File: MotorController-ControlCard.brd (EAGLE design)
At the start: 71.9 x 61 mm, 46 parts, among them J1 SL07-HORIZ, J2 SL03THROUGH_HOLE, Q7 MOSFET-PCHANNEL, Q8 MOSFET-PCHANNEL, U2 MAX3232D, U4 TMS320F28069MPZT

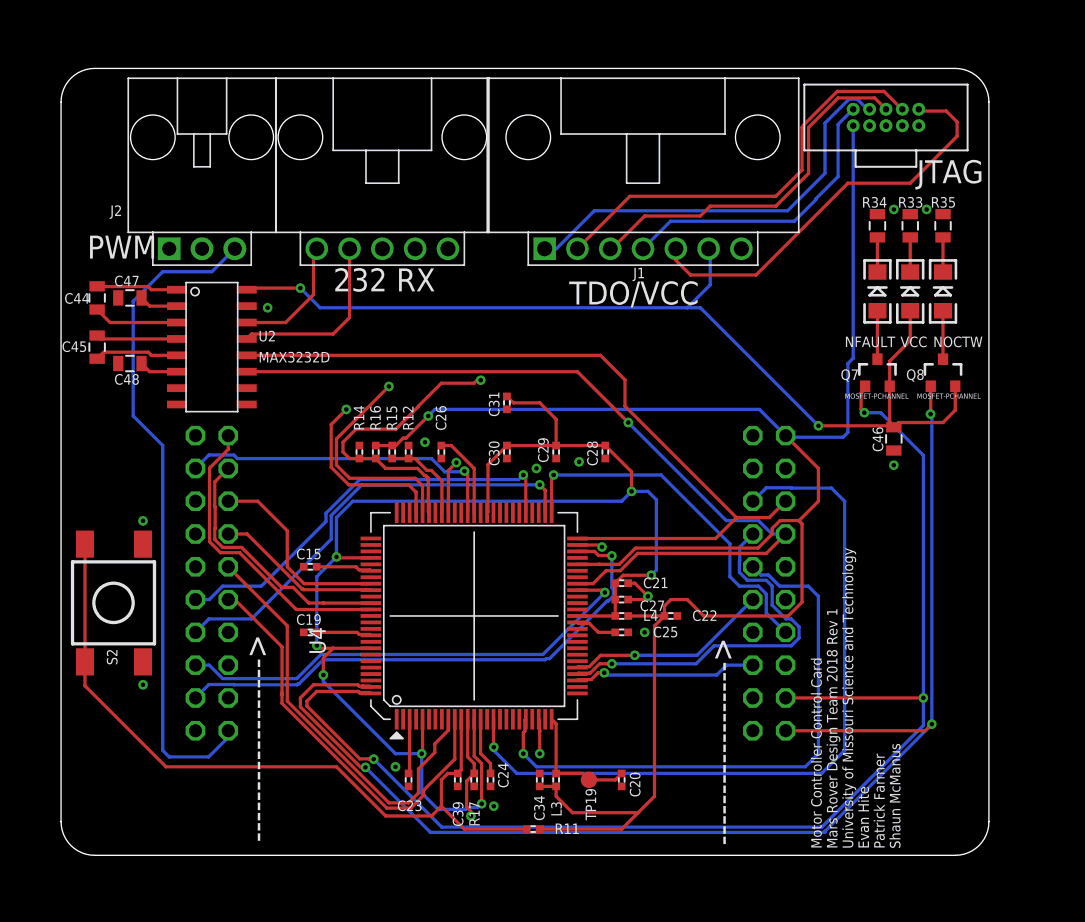
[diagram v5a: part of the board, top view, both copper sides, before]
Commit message: Routing and Silkscreen update
SL connectors were shifted apart to better mount them. Silkcreen was added around LED's for better visibility. Board was rerouted to get the board down to two layers.
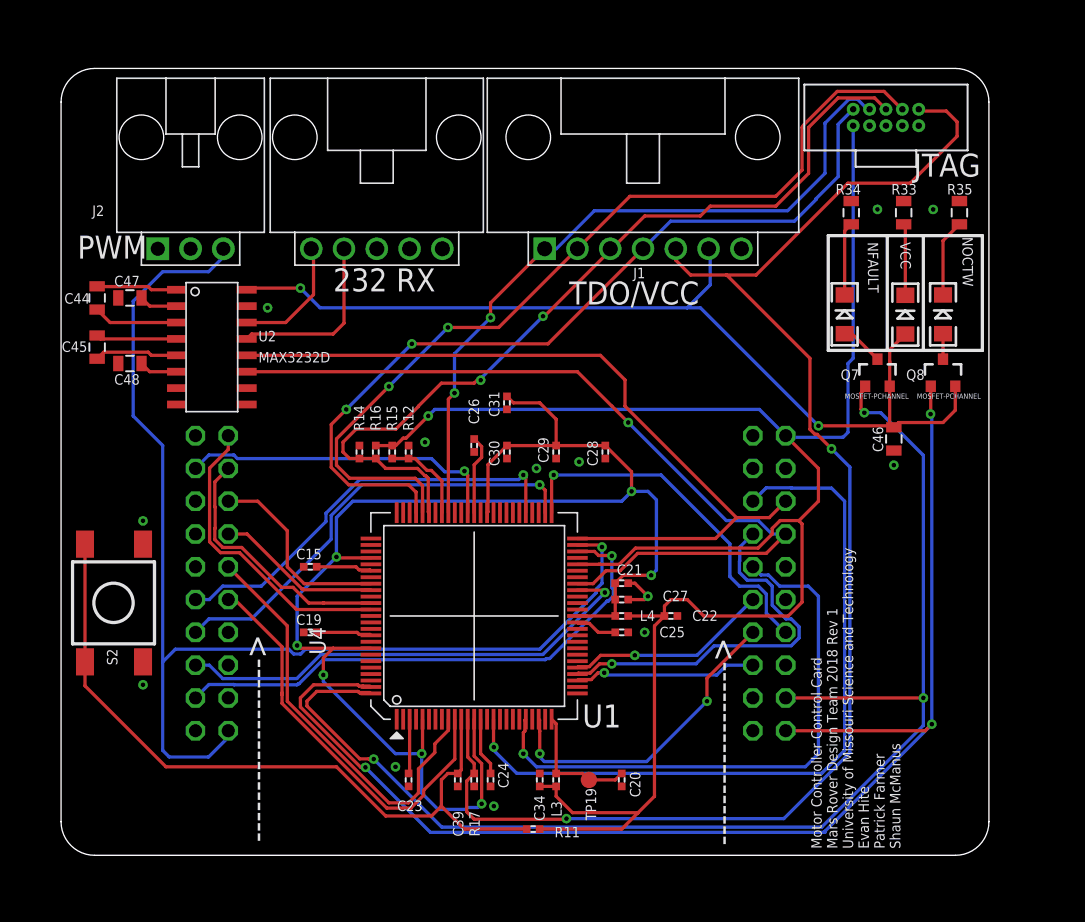
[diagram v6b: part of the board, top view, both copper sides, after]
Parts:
- moved D8 3.10 mm to (123.4, 81.3)
- moved C26 2.59 mm to (94.7, 71.1)
- moved R34 2.27 mm to (124.0, 89.2)
- moved D7 1.84 mm to (128.1, 81.3)
- moved D9 1.78 mm to (131.1, 81.3)
- moved R35 1.63 mm to (132.3, 89.2)
- moved R33 1.14 mm to (128.0, 89.2)
- moved J2 0.89 mm to (72.8, 86.4)
- moved U$4 0.43 mm to (87.2, 86.4)
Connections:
- net GND: now also U$2.7
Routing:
- net TRST: track 99.9 -> 112.8 mm, vias 1 -> 2
- net PWM_IN: track 88.6 -> 93.0 mm
- net TMS: track 69.3 -> 65.2 mm, vias 1 -> 2
- net TDI: track 72.4 -> 69.0 mm, vias 1 -> 2
- net N$27: track 2.68 -> 6.00 mm
- net N$26: track 2.68 -> 5.68 mm
- net N$24: track 2.68 -> 5.55 mm
- net VDDIO: track 113.1 -> 115.2 mm
- net SO1: track 26.7 -> 24.8 mm, vias 1 -> 2
- net N$28: track 3.75 -> 1.97 mm
- net VCC: track 77.0 -> 75.2 mm
- net N$16: track 6.70 -> 6.19 mm
- net TDO: track 66.6 -> 66.7 mm, vias 1 -> 2
- net TCK: track 56.2 -> 56.1 mm, vias 1 -> 2
- removed copper zone on layer 15, net GND
- removed copper zone on layer 2, net GND
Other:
- board text added: "U1"

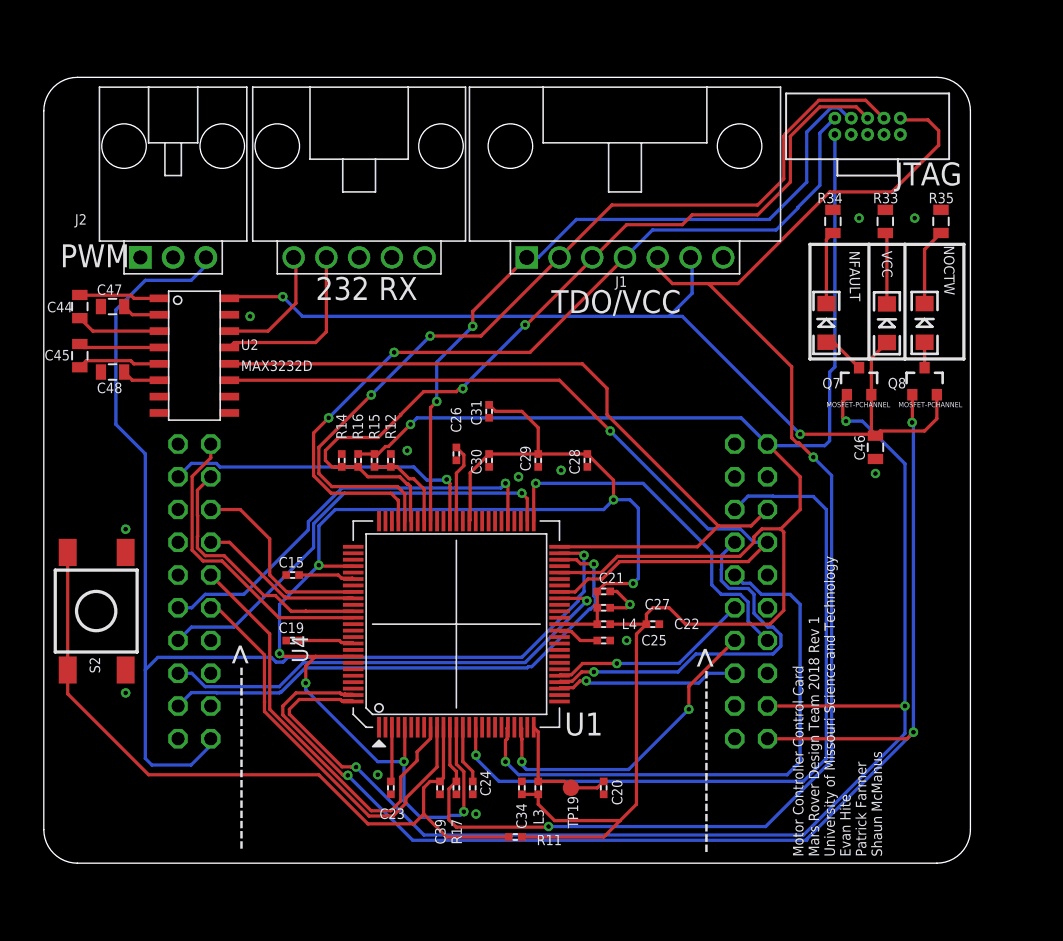
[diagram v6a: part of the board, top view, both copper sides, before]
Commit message: Removed redundant SL connector, restructured right side of board and reduced board size
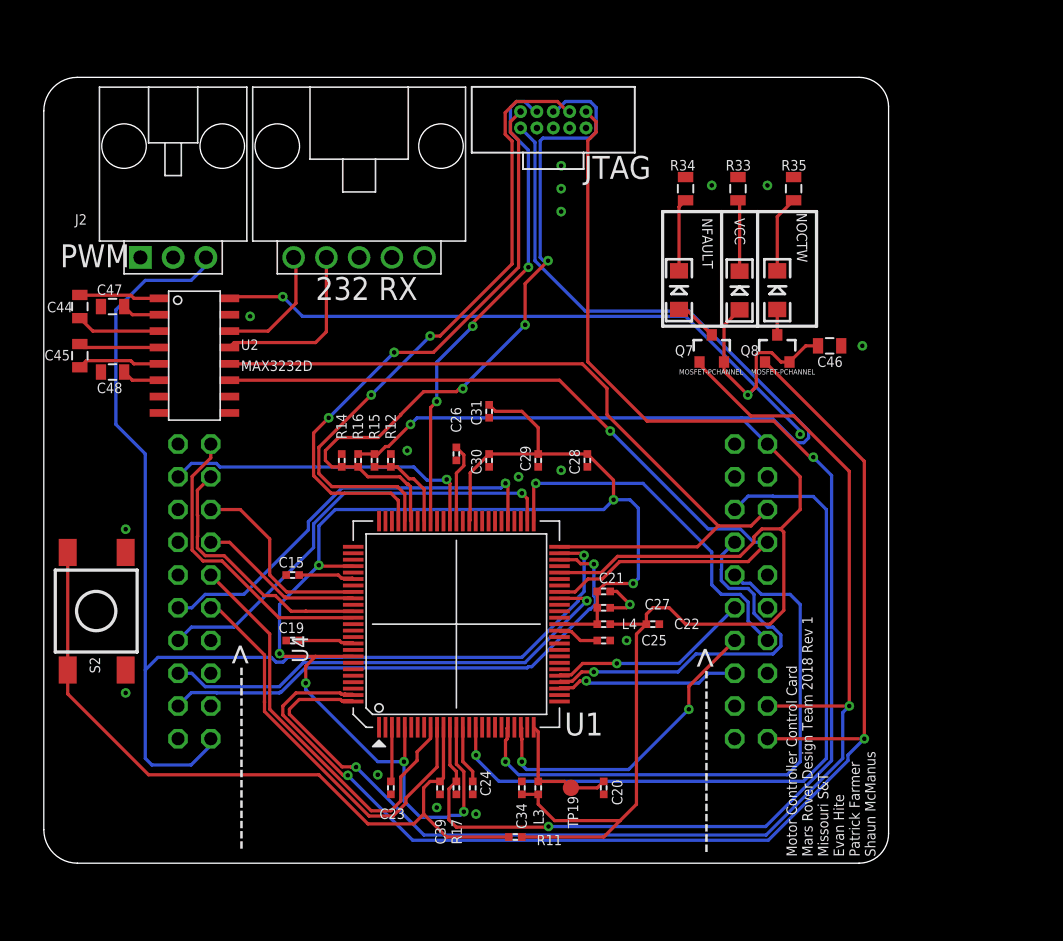
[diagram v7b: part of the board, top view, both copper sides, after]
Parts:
- removed J1: SL07-HORIZ, MRDT-Connectors:MOLEX-70551-0006
- moved U$2 24.4 mm to (108.6, 94.5)
- moved D7 11.7 mm to (116.7, 83.8)
- moved R35 11.7 mm to (120.9, 91.7)
- moved D8 11.7 mm to (112.0, 83.8)
- moved Q7 11.7 mm to (114.6, 79.2)
- moved Q8 11.7 mm to (119.6, 79.2)
- moved R33 11.7 mm to (116.6, 91.7)
- moved R34 11.7 mm to (112.5, 91.7)
- moved D9 11.7 mm to (119.6, 83.8)
- moved C46 8.64 mm to (123.7, 79.5), turned to 0 degrees
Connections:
- net GPIO34 renamed GPIO34_BOOT
- net GND: no longer J1.7
- net TCK: no longer J1.1
- net TDI: no longer J1.2
- net TDO: no longer J1.3
- net TMS: no longer J1.4
- net TRST: no longer J1.5
- net VCC: no longer J1.6
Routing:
- net TMS: track 65.2 -> 46.2 mm
- net TDI: track 69.0 -> 50.0 mm
- net TCK: track 56.1 -> 38.4 mm, vias 2 -> 3
- net +3V3: track 145.5 -> 160.7 mm
- net TDO: track 66.7 -> 56.4 mm, vias 2 -> 3
- net VCC: track 75.2 -> 66.8 mm, vias 2 -> 3
- net TRST: track 112.8 -> 104.4 mm
- net NOCTW: track 101.4 -> 99.8 mm, vias 3 -> 2
- net NFAULT: track 101.3 -> 99.9 mm, vias 3 -> 2
- net GND: vias 12 -> 16
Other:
- board size 71.9 x 61 mm -> 65.5 x 61 mm
- board text added: "Motor Controller Control Card Mars Rover Design Team 2018 Rev 1 Missouri S&T Evan Hite Patrick Farmer Shaun McManus"
- board text removed: "Motor Controller Control Card Mars Rover Design Team 2018 Rev 1 University of Missouri Science and Technology Evan Hite Patrick Farmer Shaun McManus"
- board text removed: "TDO/VCC"
